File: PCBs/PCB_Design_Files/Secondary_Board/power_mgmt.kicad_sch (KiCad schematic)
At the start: 19 parts, among them Q3 MMBT3904, Q4 MMBT3904, U2 MMSZ5221BT1G, U5 TPS61023DRLR, U6 TLV9101IDCKR

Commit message: change ldo
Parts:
- removed Q4: MMBT3904, Project Footprints:SOT23_FAS, symbol Transistor_BJT:MMBT3904
- added C9: 180p, Capacitor_SMD:C_0603_1608Metric, symbol Device:C
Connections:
- net +3V3: now also Q3.2 (E)
- net at R12.1, R13.2, U6.3 (IN-): now also C9.2
- net at R11.1, U6.4 (OUT): now also C9.1
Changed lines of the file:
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@@
-	)
-	(junction
-		(at 228.6 60.96)
-		(diameter 0)
-		(color 0 0 0 0)
 	)
 	(junction
@@
 	)
 	(junction
+		(at 204.47 78.74)
+		(diameter 0)
+		(color 0 0 0 0)
+	)
+	(junction
 		(at 29.21 77.47)
 		(diameter 0)
@@
 	)
 	(junction
+		(at 200.66 91.44)
+		(diameter 0)
+		(color 0 0 0 0)
+	)
+	(junction
 		(at 27.94 39.37)
 		(diameter 0)
@@
 	(wire
 		(pts
-			(xy 232.41 91.44) (xy 232.41 90.17)
+			(xy 232.41 85.09) (xy 232.41 91.44)
 		)
 		(stroke
@@
 	(wire
 		(pts
+			(xy 224.79 85.09) (xy 232.41 85.09)
+		)
+		(stroke
+			(width 0)
+			(type default)
+		)
+	)
+	(wire
+		(pts
 			(xy 256.54 91.44) (xy 259.08 91.44)
 		)
@@
 	(wire
 		(pts
+			(xy 204.47 88.9) (xy 204.47 91.44)
+		)
+		(stroke
+			(width 0)
+			(type default)
+		)
+	)
+	(wire
+		(pts
 			(xy 29.21 77.47) (xy 36.83 77.47)
 		)
@@
 	(wire
 		(pts
-			(xy 232.41 80.01) (xy 232.41 60.96)
-		)
-		(stroke
-			(width 0)
-			(type default)
-		)
-	)
-	(wire
-		(pts
 			(xy 91.44 93.98) (xy 73.66 93.98)
 		)
@@
 	(wire
 		(pts
+			(xy 204.47 78.74) (xy 205.74 78.74)
+		)
+		(stroke
+			(width 0)
+			(type default)
+		)
+	)
+	(wire
+		(pts
 			(xy 147.32 74.93) (xy 147.32 76.2)
 		)
@@
 	(wire
 		(pts
-			(xy 200.66 114.3) (xy 200.66 81.28)
+			(xy 200.66 81.28) (xy 200.66 91.44)
 		)
 		(stroke
@@
 	(wire
 		(pts
+			(xy 204.47 91.44) (xy 200.66 91.44)
+		)
+		(stroke
+			(width 0)
+			(type default)
+		)
+	)
+	(wire
+		(pts
 			(xy 27.94 26.67) (xy 36.83 26.67)
 		)
@@
 	(wire
 		(pts
-			(xy 200.66 78.74) (xy 205.74 78.74)
+			(xy 200.66 91.44) (xy 200.66 114.3)
+		)
+		(stroke
+			(width 0)
+			(type default)
+		)
+	)
+	(wire
+		(pts
+			(xy 200.66 78.74) (xy 204.47 78.74)
 		)
 		(stroke
@@
 	(wire
 		(pts
-			(xy 228.6 60.96) (xy 232.41 60.96)
+			(xy 204.47 78.74) (xy 204.47 81.28)
 		)
 		(stroke
@@
 				(path "/c7abdc65-9966-45f8-babc-768b62a50249"
 					(reference "R5")
-					(unit 1)
-				)
-			)
-		)
-	)
-	(symbol
-		(lib_id "Transistor_BJT:MMBT3904")
-		(at 229.87 85.09 0)
-		(unit 1)
-		(exclude_from_sim no)
-		(in_bom yes)
-		(on_board yes)
-		(dnp no)
-		(fields_autoplaced yes)
-		(property "Reference" "Q4"
-			(at 234.95 83.8199 0)
-			(effects
-				(font
-					(size 1.27 1.27)
-				)
-				(justify left)
-			)
-		)
-		(property "Value" "MMBT3904"
-			(at 234.95 86.3599 0)
-			(effects
-				(font
-					(size 1.27 1.27)
-				)
-				(justify left)
-			)
-		)
-		(property "Footprint" "Project Footprints:SOT23_FAS"
-			(at 234.95 86.995 0)
-			(effects
-				(font
-					(size 1.27 1.27)
-					(italic yes)
-				)
-				(justify left)
-				(hide yes)
-			)
-		)
-		(property "Datasheet" "https://www.onsemi.com/pdf/datasheet/pzt3904-d.pdf"
-			(at 229.87 85.09 0)
-			(effects
-				(font
-					(size 1.27 1.27)
-				)
-				(justify left)
-				(hide yes)
-			)
-		)
-		(property "Description" "0.2A Ic, 40V Vce, Small Signal NPN Transistor, SOT-23"
-			(at 229.87 85.09 0)
-			(effects
-				(font
-					(size 1.27 1.27)
-				)
-				(hide yes)
-			)
-		)
-		(pin "2"
-		)
-		(pin "1"
-		)
-		(pin "3"
-		)
-		(instances
-			(project "Secondary_Board"
-				(path "/2f5986e4-77b2-4f5d-ab91-80ba6228eb8b/3db8306c-5846-4ae5-ba17-fe529edf9e71"
-					(reference "Q4")
-					(unit 1)
-				)
-			)
-			(project "power_mgmt"
-				(path "/c7abdc65-9966-45f8-babc-768b62a50249"
-					(reference "Q4")
 					(unit 1)
 				)
@@
 					(unit 1)
 				)
+			)
+		)
+	)
+	(symbol
+		(lib_id "Device:C")
+		(at 204.47 85.09 0)
+		(unit 1)
+		(exclude_from_sim no)
+		(in_bom yes)
+		(on_board yes)
+		(dnp no)
+		(fields_autoplaced yes)
+		(property "Reference" "C9"
+			(at 208.28 83.8199 0)
+			(effects
+				(font
+					(size 1.27 1.27)
+				)
+				(justify left)
+			)
+		)
+		(property "Value" "180p"
+			(at 208.28 86.3599 0)
+			(effects
+				(font
+					(size 1.27 1.27)
+				)
+				(justify left)
+			)
+		)
+		(property "Footprint" "Capacitor_SMD:C_0603_1608Metric"
+			(at 205.4352 88.9 0)
+			(effects
+				(font
+					(size 1.27 1.27)
+				)
+				(hide yes)
+			)
+		)
+		(property "Datasheet" "~"
+			(at 204.47 85.09 0)
+			(effects
+				(font
+					(size 1.27 1.27)
+				)
+				(hide yes)
+			)
+		)
+		(property "Description" "Unpolarized capacitor"
+			(at 204.47 85.09 0)
+			(effects
+				(font
+					(size 1.27 1.27)
+				)
+				(hide yes)
+			)
+		)
+		(pin "2"
+		)
+		(pin "1"
+		)
+		(instances
+			(project "Secondary_Board"
+				(path "/2f5986e4-77b2-4f5d-ab91-80ba6228eb8b/3db8306c-5846-4ae5-ba17-fe529edf9e71"
+					(reference "C9")
+					(unit 1)
+				)

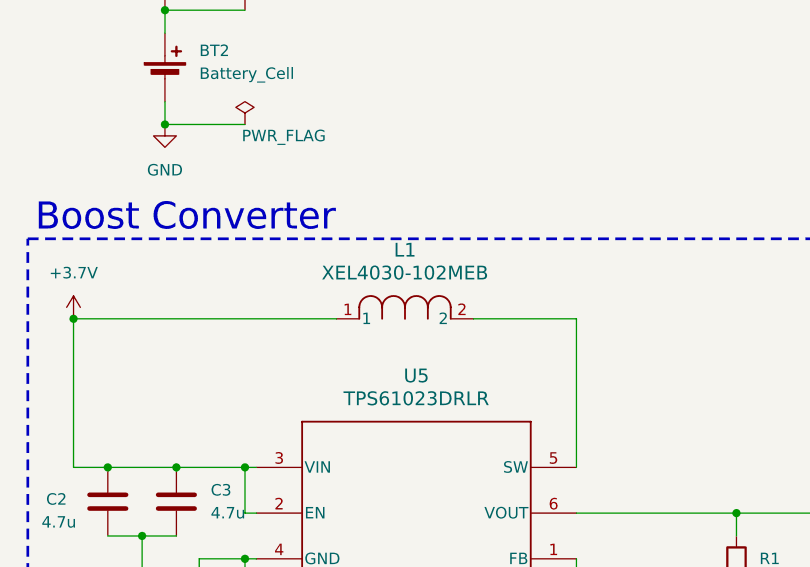
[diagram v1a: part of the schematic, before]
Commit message: added symbols
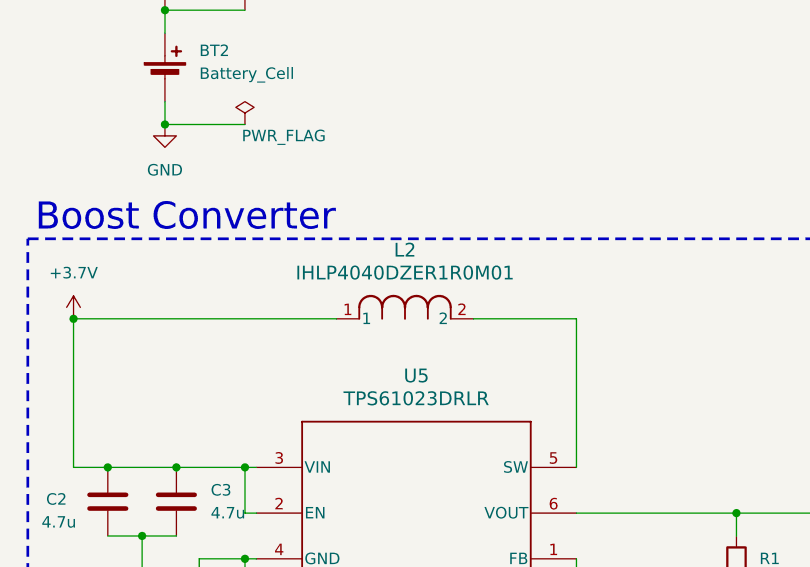
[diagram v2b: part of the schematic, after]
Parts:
- removed L1: XEL4030-102MEB, Project Footprints:IND_XEL4030_3.1_COC, symbol Project_Symbols:XEL4030-102MEB
- added L2: IHLP4040DZER1R0M01, Project Footprints:IND_IHLP-4040DZ_VIS, symbol Project_Symbols:IHLP4040DZER1R0M01
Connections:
- net +3.7V: now also L2.1
- net at U5.5 (SW): now also L2.2
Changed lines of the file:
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@@
 	)
 	(symbol
-		(lib_id "Project_Symbols:XEL4030-102MEB")
-		(at 62.23 60.96 0)
-		(mirror y)
+		(lib_id "Project_Symbols:IHLP4040DZER1R0M01")
+		(at 46.99 60.96 0)
 		(unit 1)
 		(exclude_from_sim no)
@@
 		(on_board yes)
 		(dnp no)
-		(property "Reference" "L1"
+		(fields_autoplaced yes)
+		(property "Reference" "L2"
 			(at 54.61 53.34 0)
 			(effects
@@
 			)
 		)
-		(property "Value" "XEL4030-102MEB"
+		(property "Value" "IHLP4040DZER1R0M01"
 			(at 54.61 55.88 0)
 			(effects
@@
 			)
 		)
-		(property "Footprint" "Project Footprints:IND_XEL4030_3.1_COC"
-			(at 62.23 60.96 0)
+		(property "Footprint" "Project Footprints:IND_IHLP-4040DZ_VIS"
+			(at 56.388 66.04 0)
 			(effects
 				(font
@@
 			)
 		)
-		(property "Datasheet" "XEL4030-102MEB"
-			(at 62.23 60.96 0)
+		(property "Datasheet" "https://www.vishay.com/doc?34193"
+			(at 57.15 65.786 0)
 			(effects
 				(font
@@
 		)
 		(property "Description" ""
-			(at 62.23 60.96 0)
+			(at 46.99 60.96 0)
 			(effects
 				(font
@@
 			(project ""
 				(path "/2f5986e4-77b2-4f5d-ab91-80ba6228eb8b/3db8306c-5846-4ae5-ba17-fe529edf9e71"
-					(reference "L1")
+					(reference "L2")
 					(unit 1)
 				)

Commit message: update inductor
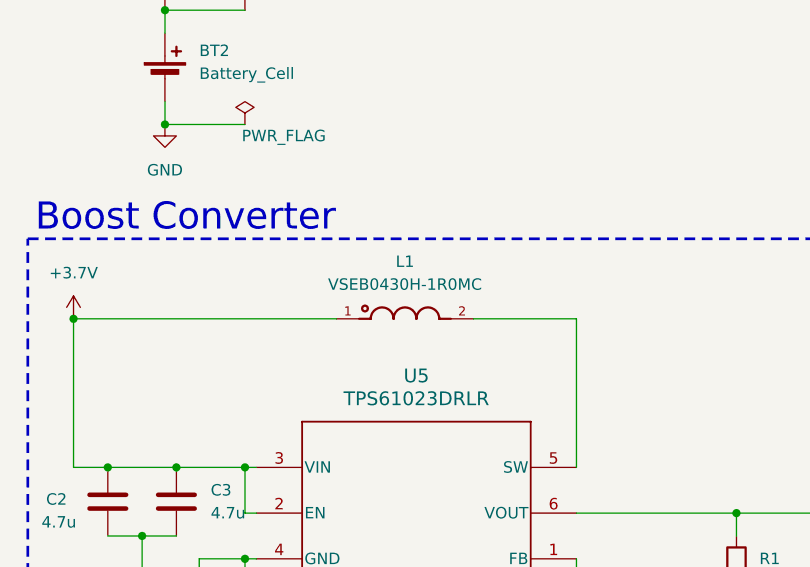
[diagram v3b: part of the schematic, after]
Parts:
- removed L2: IHLP4040DZER1R0M01, Project Footprints:IND_IHLP-4040DZ_VIS, symbol Project_Symbols:IHLP4040DZER1R0M01
- added L1: VSEB0430H-1R0MC, Project Footprints:IND_VSEB0430H-1R0MC, symbol Project_Symbols:VSEB0430H-1R0MC
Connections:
- net +3.7V: now also L1.1
- net at U5.5 (SW): now also L1.2
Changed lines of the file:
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@@
-	)
-	(symbol
-		(lib_id "Project_Symbols:IHLP4040DZER1R0M01")
-		(at 46.99 60.96 0)
-		(unit 1)
-		(exclude_from_sim no)
-		(in_bom yes)
-		(on_board yes)
-		(dnp no)
-		(fields_autoplaced yes)
-		(property "Reference" "L2"
-			(at 54.61 53.34 0)
-			(effects
-				(font
-					(size 1.524 1.524)
-				)
-			)
-		)
-		(property "Value" "IHLP4040DZER1R0M01"
-			(at 54.61 55.88 0)
-			(effects
-				(font
-					(size 1.524 1.524)
-				)
-			)
-		)
-		(property "Footprint" "Project Footprints:IND_IHLP-4040DZ_VIS"
-			(at 56.388 66.04 0)
-			(effects
-				(font
-					(size 1.27 1.27)
-					(italic yes)
-				)
-				(hide yes)
-			)
-		)
-		(property "Datasheet" "https://www.vishay.com/doc?34193"
-			(at 57.15 65.786 0)
-			(effects
-				(font
-					(size 1.27 1.27)
-					(italic yes)
-				)
-				(hide yes)
-			)
-		)
-		(property "Description" ""
-			(at 46.99 60.96 0)
-			(effects
-				(font
-					(size 1.27 1.27)
-				)
-				(hide yes)
-			)
-		)
-		(pin "1"
-		)
-		(pin "2"
-		)
-		(instances
-			(project ""
-				(path "/2f5986e4-77b2-4f5d-ab91-80ba6228eb8b/3db8306c-5846-4ae5-ba17-fe529edf9e71"
-					(reference "L2")
-					(unit 1)
-				)
-			)
-		)
 	)
 	(symbol
@@
 					(unit 1)
 				)
+			)
+		)
+	)
+	(symbol
+		(lib_id "Project_Symbols:VSEB0430H-1R0MC")
+		(at 54.61 60.96 0)
+		(unit 1)
+		(exclude_from_sim no)
+		(in_bom yes)
+		(on_board yes)
+		(dnp no)
+		(fields_autoplaced yes)
+		(property "Reference" "L1"
+			(at 54.61 54.61 0)
+			(effects
+				(font
+					(size 1.27 1.27)
+				)
+			)
+		)
+		(property "Value" "VSEB0430H-1R0MC"
+			(at 54.61 57.15 0)
+			(effects
+				(font
+					(size 1.27 1.27)
+				)
+			)
+		)
+		(property "Footprint" "Project Footprints:IND_VSEB0430H-1R0MC"
+			(at 54.61 65.024 0)
+			(effects
+				(font
+					(size 1.27 1.27)
+				)
+				(justify bottom)
+				(hide yes)
+			)
+		)
+		(property "Datasheet" ""
+			(at 54.61 60.96 0)
+			(effects
+				(font
+					(size 1.27 1.27)
+				)
+				(hide yes)
+			)
+		)
+		(property "Description" ""
+			(at 54.61 60.96 0)
+			(effects
+				(font
+					(size 1.27 1.27)
+				)
+				(hide yes)
+			)
+		)
+		(property "MF" "CODACA"
+			(at 54.61 63.5 0)
+			(effects
+				(font
+					(size 1.27 1.27)
+				)
+				(justify bottom)
+				(hide yes)
+			)
+		)
+		(property "MAXIMUM_PACKAGE_HEIGHT" "3.20mm"
+			(at 54.102 64.262 0)
+			(effects
+				(font
+					(size 1.27 1.27)
+				)
+				(justify bottom)
+				(hide yes)
+			)
+		)
+		(property "CREATOR" "RODRIGO"
+			(at 54.61 63.5 0)
+			(effects
+				(font
+					(size 1.27 1.27)
+				)
+				(justify bottom)
+				(hide yes)
+			)
+		)
+		(property "Price" "None"
+			(at 54.61 64.262 0)
+			(effects
+				(font
+					(size 1.27 1.27)
+				)
+				(justify bottom)
+				(hide yes)
+			)
+		)
+		(property "Package" "None"
+			(at 54.61 66.294 0)
+			(effects
+				(font
+					(size 1.27 1.27)
+				)
+				(justify bottom)
+				(hide yes)
+			)
+		)
+		(property "Check_prices" "https://www.snapeda.com/parts/VSEB0430H-1R0MC/Codaca/view-part/?ref=eda"
+			(at 54.61 65.024 0)
+			(effects
+				(font
+					(size 1.27 1.27)
+				)
+				(justify bottom)
+				(hide yes)
+			)
+		)
+		(property "STANDARD" "IPC-7351B"
+			(at 54.102 65.532 0)
+			(effects
+				(font
+					(size 1.27 1.27)
+				)
+				(justify bottom)
+				(hide yes)
+			)
+		)
+		(property "PARTREV" "09/15/2025"
+			(at 54.864 65.024 0)
+			(effects
+				(font
+					(size 1.27 1.27)
+				)
+				(justify bottom)
+				(hide yes)
+			)
+		)
+		(property "VERIFIER" ""
+			(at 54.61 60.96 0)
+			(effects
+				(font
+					(size 1.27 1.27)
+				)
+				(justify bottom)
+				(hide yes)
+			)
+		)
+		(property "SnapEDA_Link" "https://www.snapeda.com/parts/VSEB0430H-1R0MC/Codaca/view-part/?ref=snap"
+			(at 54.864 65.024 0)
+			(effects
+				(font
+					(size 1.27 1.27)
+				)
+				(justify bottom)
+				(hide yes)
+			)
+		)
+		(property "MP" "VSEB0430H-1R0MC"
+			(at 55.118 62.992 0)
+			(effects
+				(font
+					(size 1.27 1.27)
+				)
+				(justify bottom)
+				(hide yes)
+			)
+		)
+		(property "Description_1" "1 µH Shielded Molded Inductor 10.7 A 10.3mOhm Max 2-SMD Molded Inductors, Automotive Grade Power Inductors"
+			(at 54.356 64.77 0)
+			(effects
+				(font
+					(size 1.27 1.27)
+				)
+				(justify bottom)
+				(hide yes)
+			)
+		)
+		(property "Availability" "In Stock"
+			(at 54.61 63.754 0)
+			(effects
+				(font
+					(size 1.27 1.27)
+				)
+				(justify bottom)
+				(hide yes)
+			)
+		)
+		(property "MANUFACTURER" "Codaca"
+			(at 54.61 62.484 0)
+			(effects
+				(font
+					(size 1.27 1.27)
+				)
+				(justify bottom)
+				(hide yes)
+			)
+		)
+		(pin "2"
+		)
+		(pin "1"
+		)
+		(instances
+			(project ""
+				(path "/2f5986e4-77b2-4f5d-ab91-80ba6228eb8b/3db8306c-5846-4ae5-ba17-fe529edf9e71"
+					(reference "L1")
+					(unit 1)
+				)

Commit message: switch
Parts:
- added SW1: SW_Nidec_CAS-120A1, Button_Switch_SMD:Nidec_Copal_CAS-120A, symbol Switch:SW_Nidec_CAS-120A1
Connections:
- net +3.7V: now also SW1.1 (C); no longer U5.2 (EN)
- net GND: now also SW1.3 (A)
- new net: SW1.2 (B), U5.2 (EN)
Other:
- moved on the sheet: C2, C3, U5
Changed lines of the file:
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@@
 	)
 	(junction
+		(at 25.4 77.47)
+		(diameter 0)
+		(color 0 0 0 0)
+	)
+	(junction
 		(at 123.19 82.55)
 		(diameter 0)
@@
 	)
 	(junction
+		(at 17.78 77.47)
+		(diameter 0)
+		(color 0 0 0 0)
+	)
+	(junction
 		(at 91.44 93.98)
 		(diameter 0)
@@
 	)
 	(junction
+		(at 34.29 87.63)
+		(diameter 0)
+		(color 0 0 0 0)
+	)
+	(junction
 		(at 256.54 91.44)
 		(diameter 0)
@@
 	)
 	(junction
+		(at 80.01 82.55)
+		(diameter 0)
+		(color 0 0 0 0)
+	)
+	(junction
 		(at 236.22 91.44)
 		(diameter 0)
@@
 	)
 	(junction
-		(at 29.21 77.47)
+		(at 33.02 77.47)
 		(diameter 0)
 		(color 0 0 0 0)
@@
 	)
 	(junction
-		(at 25.4 85.09)
-		(diameter 0)
-		(color 0 0 0 0)
-	)
-	(junction
-		(at 21.59 77.47)
+		(at 21.59 85.09)
 		(diameter 0)
 		(color 0 0 0 0)
@@
 	)
 	(junction
-		(at 36.83 77.47)
-		(diameter 0)
-		(color 0 0 0 0)
-	)
-	(junction
 		(at 91.44 110.49)
 		(diameter 0)
@@
 	(wire
 		(pts
-			(xy 73.66 82.55) (xy 91.44 82.55)
+			(xy 73.66 82.55) (xy 80.01 82.55)
 		)
 		(stroke
@@
 	(wire
 		(pts
-			(xy 73.66 93.98) (xy 73.66 87.63)
+			(xy 80.01 93.98) (xy 80.01 87.63)
 		)
 		(stroke
@@
 	(wire
 		(pts
-			(xy 31.75 87.63) (xy 36.83 87.63)
+			(xy 31.75 87.63) (xy 34.29 87.63)
 		)
 		(stroke
@@
 	(wire
 		(pts
-			(xy 73.66 60.96) (xy 73.66 77.47)
+			(xy 80.01 60.96) (xy 80.01 77.47)
 		)
 		(stroke
@@
 	(wire
 		(pts
-			(xy 62.23 60.96) (xy 73.66 60.96)
+			(xy 62.23 60.96) (xy 80.01 60.96)
 		)
 		(stroke
@@
 	(wire
 		(pts
-			(xy 21.59 77.47) (xy 29.21 77.47)
-		)
-		(stroke
-			(width 0)
-			(type default)
-		)
-	)
-	(wire
-		(pts
 			(xy 123.19 90.17) (xy 123.19 110.49)
 		)
@@
 	(wire
 		(pts
-			(xy 25.4 85.09) (xy 25.4 88.9)
+			(xy 21.59 85.09) (xy 21.59 88.9)
+		)
+		(stroke
+			(width 0)
+			(type default)
+		)
+	)
+	(wire
+		(pts
+			(xy 33.02 77.47) (xy 44.45 77.47)
+		)
+		(stroke
+			(width 0)
+			(type default)
+		)
+	)
+	(wire
+		(pts
+			(xy 33.02 80.01) (xy 33.02 77.47)
 		)
 		(stroke
@@
 	(wire
 		(pts
-			(xy 36.83 77.47) (xy 38.1 77.47)
+			(xy 25.4 77.47) (xy 33.02 77.47)
 		)
 		(stroke
@@
 	(wire
 		(pts
-			(xy 29.21 77.47) (xy 36.83 77.47)
+			(xy 34.29 87.63) (xy 36.83 87.63)
 		)
 		(stroke
@@
 	(wire
 		(pts
-			(xy 91.44 93.98) (xy 73.66 93.98)
+			(xy 91.44 93.98) (xy 80.01 93.98)
 		)
 		(stroke
@@
 	(wire
 		(pts
-			(xy 38.1 82.55) (xy 36.83 82.55)
+			(xy 245.11 115.57) (xy 250.19 115.57)
 		)
 		(stroke
@@
 	(wire
 		(pts
-			(xy 245.11 115.57) (xy 250.19 115.57)
+			(xy 34.29 85.09) (xy 34.29 87.63)
 		)
 		(stroke
@@
 	(wire
 		(pts
-			(xy 21.59 85.09) (xy 25.4 85.09)
+			(xy 17.78 85.09) (xy 21.59 85.09)
 		)
 		(stroke
@@
 	(wire
 		(pts
-			(xy 25.4 85.09) (xy 29.21 85.09)
+			(xy 21.59 85.09) (xy 25.4 85.09)
 		)
 		(stroke
@@
 	(wire
 		(pts
-			(xy 36.83 87.63) (xy 38.1 87.63)
+			(xy 34.29 80.01) (xy 33.02 80.01)
+		)
+		(stroke
+			(width 0)
+			(type default)
+		)
+	)
+	(wire
+		(pts
+			(xy 36.83 87.63) (xy 44.45 87.63)
 		)
 		(stroke
@@
 	(wire
 		(pts
-			(xy 17.78 77.47) (xy 21.59 77.47)
+			(xy 17.78 77.47) (xy 25.4 77.47)
 		)
 		(stroke
@@
 	(wire
 		(pts
-			(xy 36.83 77.47) (xy 36.83 82.55)
+			(xy 80.01 82.55) (xy 91.44 82.55)
 		)
 		(stroke
@@
 	(symbol
 		(lib_id "power:GND")
-		(at 25.4 88.9 0)
+		(at 21.59 88.9 0)
 		(unit 1)
 		(exclude_from_sim no)
@@
 		(fields_autoplaced yes)
 		(property "Reference" "#PWR0109"
-			(at 25.4 95.25 0)
+			(at 21.59 95.25 0)
 			(effects
 				(font
@@
 		)
 		(property "Value" "GND"
-			(at 25.4 93.98 0)
+			(at 21.59 93.98 0)
 			(effects
 				(font
@@
 		)
 		(property "Footprint" ""
-			(at 25.4 88.9 0)
+			(at 21.59 88.9 0)
 			(effects
 				(font
@@
 		)
 		(property "Datasheet" ""
-			(at 25.4 88.9 0)
+			(at 21.59 88.9 0)
 			(effects
 				(font
@@
 		)
 		(property "Description" "Power symbol creates a global label with name \"GND\" , ground"
-			(at 25.4 88.9 0)
+			(at 21.59 88.9 0)
 			(effects
 				(font
@@
 	)
 	(symbol
+		(lib_id "Switch:SW_Nidec_CAS-120A1")
+		(at 39.37 82.55 180)
+		(unit 1)
+		(exclude_from_sim no)
+		(in_bom yes)
+		(on_board yes)
+		(dnp no)
+		(fields_autoplaced yes)
+		(property "Reference" "SW1"
+			(at 39.37 73.66 0)
+			(effects
+				(font
+					(size 1.27 1.27)
+				)
+			)
+		)
+		(property "Value" "SW_Nidec_CAS-120A1"
+			(at 39.37 76.2 0)
+			(effects
+				(font
+					(size 1.27 1.27)
+				)
+			)
+		)
+		(property "Footprint" "Button_Switch_SMD:Nidec_Copal_CAS-120A"
+			(at 39.37 72.39 0)
+			(effects
+				(font
+					(size 1.27 1.27)
+				)
+				(hide yes)
+			)
+		)
+		(property "Datasheet" "https://www.nidec-components.com/e/catalog/switch/cas.pdf"
+			(at 39.37 74.93 0)
+			(effects
+				(font
+					(size 1.27 1.27)
+				)
+				(hide yes)
+			)
+		)
+		(property "Description" "Switch, single pole double throw"
+			(at 39.37 82.55 0)
+			(effects
+				(font
+					(size 1.27 1.27)
+				)
+				(hide yes)
+			)
+		)
+		(pin "2"
+		)
+		(pin "1"
+		)
+		(pin "3"
+		)
+		(instances
+			(project ""
+				(path "/2f5986e4-77b2-4f5d-ab91-80ba6228eb8b/3db8306c-5846-4ae5-ba17-fe529edf9e71"
+					(reference "SW1")
+					(unit 1)
+				)
+			)
+		)
+	)
+	(symbol
 		(lib_id "Device:R")
 		(at 209.55 78.74 90)
@@
 	(symbol
 		(lib_id "Project_Symbols:TPS61023DRLR")
-		(at 55.88 82.55 0)
+		(at 62.23 82.55 0)
 		(unit 1)
 		(exclude_from_sim no)
@@
 		(fields_autoplaced yes)
 		(property "Reference" "U5"
-			(at 55.88 67.31 0)
+			(at 62.23 67.31 0)
 			(effects
 				(font
@@
 		)
 		(property "Value" "TPS61023DRLR"
-			(at 55.88 69.85 0)
+			(at 62.23 69.85 0)
 			(effects
 				(font
@@
 		)
 		(property "Footprint" "Project Footprints:DRL0006A"
-			(at 55.372 95.25 0)
+			(at 61.722 95.25 0)
 			(effects
 				(font
@@
 		)
 		(property "Datasheet" "https://www.ti.com/lit/gpn/tps61023"
-			(at 57.15 93.472 0)
+			(at 63.5 93.472 0)
 			(effects
 				(font
@@
 		)
 		(property "Description" ""
-			(at 55.88 82.55 0)
+			(at 62.23 82.55 0)
 			(effects
 				(font
@@
 	(symbol
 		(lib_id "Device:C")
-		(at 21.59 81.28 0)
+		(at 17.78 81.28 0)
 		(unit 1)
 		(exclude_from_sim no)
@@
 		(dnp no)
 		(property "Reference" "C2"
-			(at 14.732 81.026 0)
+			(at 10.922 81.026 0)
 			(effects
 				(font
@@
 		)
 		(property "Value" "4.7u"
-			(at 14.224 83.566 0)
+			(at 10.414 83.566 0)
 			(effects
 				(font
@@
 		)
 		(property "Footprint" "Capacitor_SMD:C_0603_1608Metric"
-			(at 22.5552 85.09 0)
+			(at 18.7452 85.09 0)
 			(effects
 				(font
@@
 		)
 		(property "Datasheet" "~"
-			(at 21.59 81.28 0)
+			(at 17.78 81.28 0)
 			(effects
 				(font
@@
 		)
 		(property "Description" "Unpolarized capacitor"
-			(at 21.59 81.28 0)
+			(at 17.78 81.28 0)
 			(effects
 				(font
@@
 	(symbol
 		(lib_id "Device:C")
-		(at 29.21 81.28 0)
+		(at 25.4 81.28 0)
 		(unit 1)
 		(exclude_from_sim no)
@@
 		(fields_autoplaced yes)
 		(property "Reference" "C3"
-			(at 33.02 80.0099 0)
+			(at 29.21 80.0099 0)
 			(effects
 				(font
@@
 		)
 		(property "Value" "4.7u"
-			(at 33.02 82.5499 0)
+			(at 29.21 82.5499 0)
 			(effects
 				(font
@@
 		)
 		(property "Footprint" "Capacitor_SMD:C_0603_1608Metric"
-			(at 30.1752 85.09 0)
+			(at 26.3652 85.09 0)
 			(effects
 				(font
@@
 		)
 		(property "Datasheet" "~"
-			(at 29.21 81.28 0)
+			(at 25.4 81.28 0)
 			(effects
 				(font
@@
 		)
 		(property "Description" "Unpolarized capacitor"
-			(at 29.21 81.28 0)
+			(at 25.4 81.28 0)
 			(effects
 				(font

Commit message: connector added
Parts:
- removed SW1: SW_Nidec_CAS-120A1, Button_Switch_SMD:Nidec_Copal_CAS-120A, symbol Switch:SW_Nidec_CAS-120A1
- added J2: Conn_01x03_Pin, symbol Connector:Conn_01x03_Pin
- added R21: 100k, Project Footprints:0603_resistor, symbol Device:R
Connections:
- net +3.7V: now also J2.1 (Pin_1)
- net GND: now also R21.2
- net at U5.2 (EN): now also J2.2 (Pin_2)
- new net: J2.3 (Pin_3), R21.1

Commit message: added switch
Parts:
- J2: footprint (none) -> Connector_PinHeader_2.54mm:PinHeader_1x03_P2.54mm_Vertical
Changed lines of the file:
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@@
 			)
 		)
-		(property "Footprint" ""
+		(property "Footprint" "Connector_PinHeader_2.54mm:PinHeader_1x03_P2.54mm_Vertical"
 			(at 34.29 83.82 0)
 			(effects
